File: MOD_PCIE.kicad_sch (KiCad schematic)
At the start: 1 part, among them J6 Bus_PCI_Express_Mini

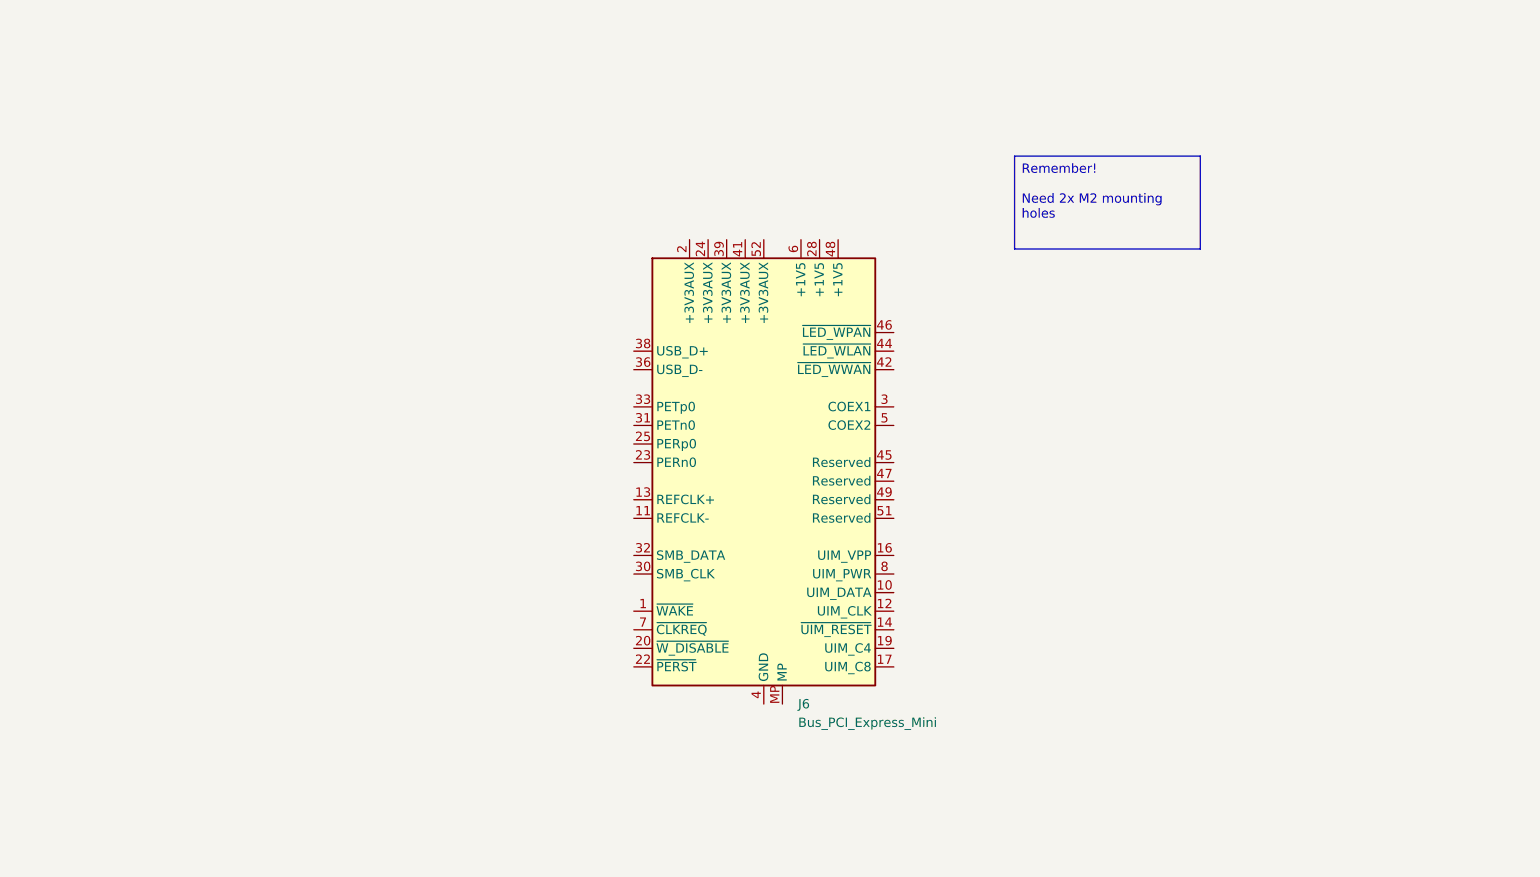
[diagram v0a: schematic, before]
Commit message: routed more sheets, improved analogs. next 5v /analog ground
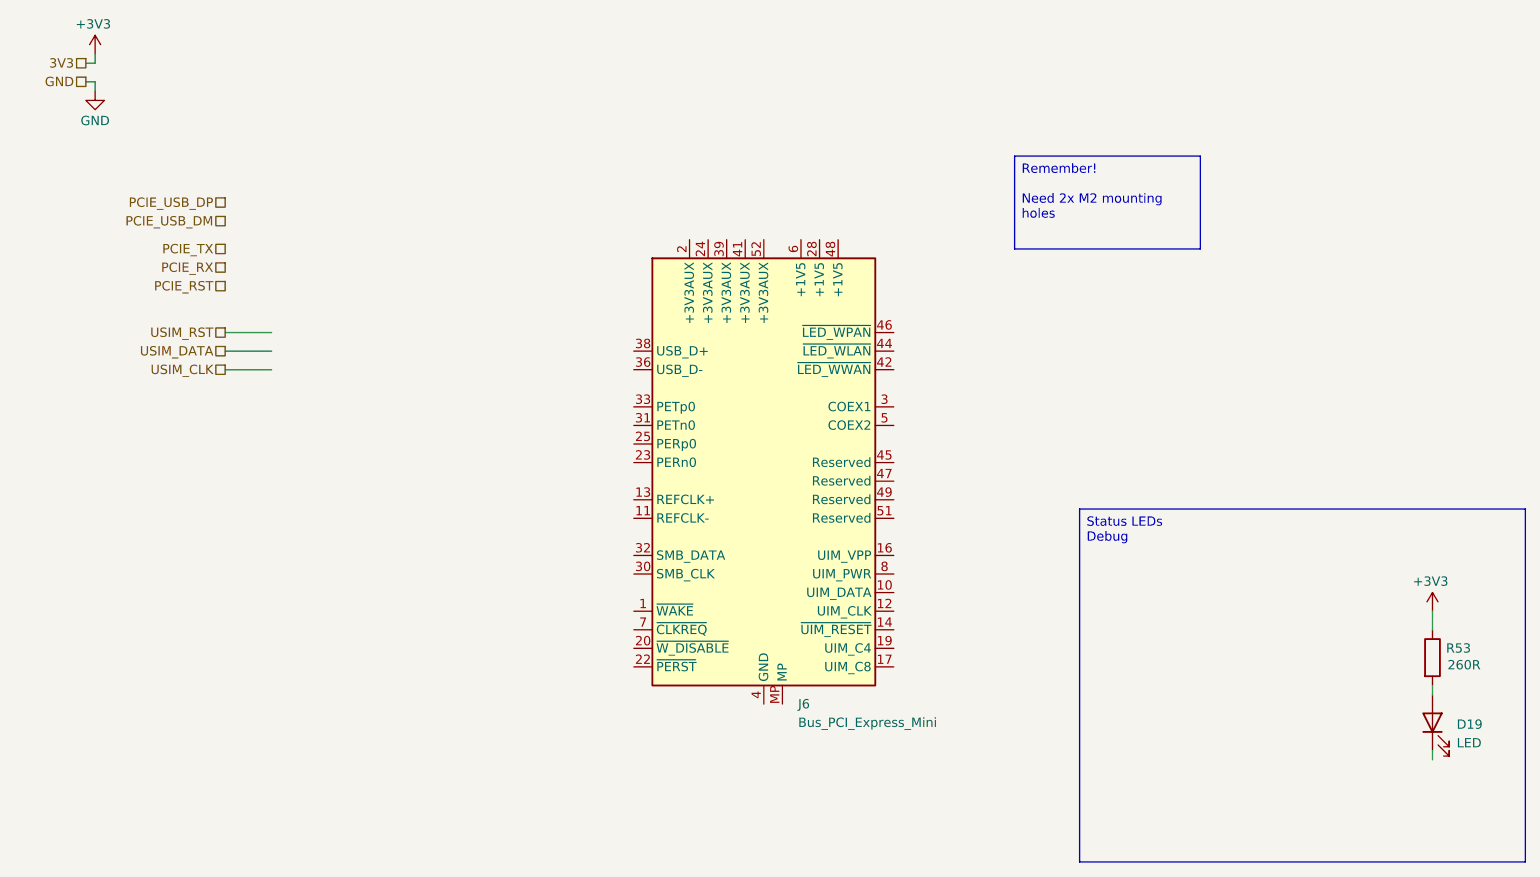
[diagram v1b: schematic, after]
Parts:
- added D19: LED, LED_SMD:LED_0603_1608Metric_Pad1.05x0.95mm_HandSolder, symbol Device:LED
- added R53: 260R, Resistor_SMD:R_0603_1608Metric_Pad0.98x0.95mm_HandSolder, symbol Device:R
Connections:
- new net: D19.2 (A), R53.2
- new net +3V3: R53.1

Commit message: added dip switches to wireless disables
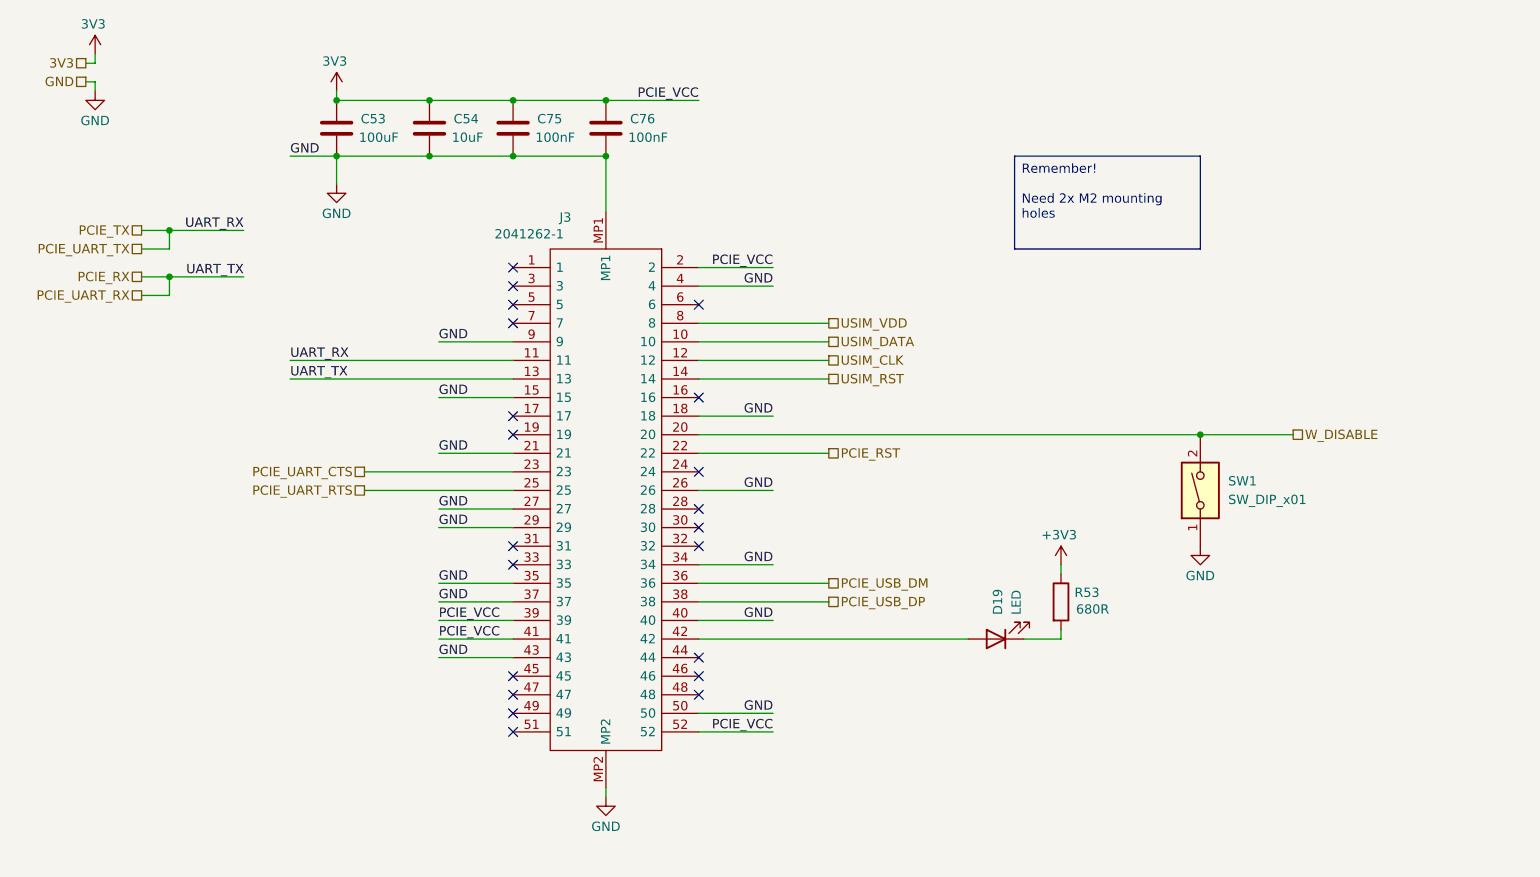
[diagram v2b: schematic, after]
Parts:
- removed J6: Bus_PCI_Express_Mini, Connector_PCBEdge:BUS_PCI_Express_Mini_Full, symbol Connector:Bus_PCI_Express_Mini
- added C53: 100uF, Capacitor_SMD:C_1210_3225Metric_Pad1.33x2.70mm_HandSolder, symbol Device:C
- added C54: 10uF, Capacitor_SMD:C_0603_1608Metric_Pad1.08x0.95mm_HandSolder, symbol Device:C
- added C75, C76: 100nF, Capacitor_SMD:C_0603_1608Metric_Pad1.08x0.95mm_HandSolder, symbol Device:C
- added J3: 2041262-1, 20412621, symbol 0_SamacSys_Parts:2041262-1
- added SW1: SW_DIP_x01, symbol Switch:SW_DIP_x01
- R53: value 260R -> 680R
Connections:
- net GND: now also C53.2, C54.2, C75.2, C76.2, J3.15, J3.18, J3.21, J3.26, J3.27, J3.29, J3.34, J3.35, J3.37, J3.4, J3.40, J3.43, J3.50, J3.9, J3.MP1, J3.MP2, SW1.1
- net PCIE_RST: now also J3.22
- net PCIE_RX: now also J3.13
- net PCIE_TX: now also J3.11
- net PCIE_USB_DM: now also J3.36
- net PCIE_USB_DP: now also J3.38
- net USIM_CLK: now also J3.12
- net USIM_DATA: now also J3.10
- net USIM_RST: now also J3.14
- net at D19.1 (K): now also R53.2
- net at D19.2 (A): now also J3.42; no longer R53.2
- new net 3V3: C53.1, C54.1, C75.1, C76.1, J3.2, J3.39, J3.41, J3.52
- new net PCIE_UART_CTS: J3.23
- new net PCIE_UART_RTS: J3.25
- new net USIM_VDD: J3.8
- new net W_DISABLE: J3.20, SW1.2
- no-connect marks 0 -> 21
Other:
- moved on the sheet: D19, R53

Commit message: redid annotations, added test point
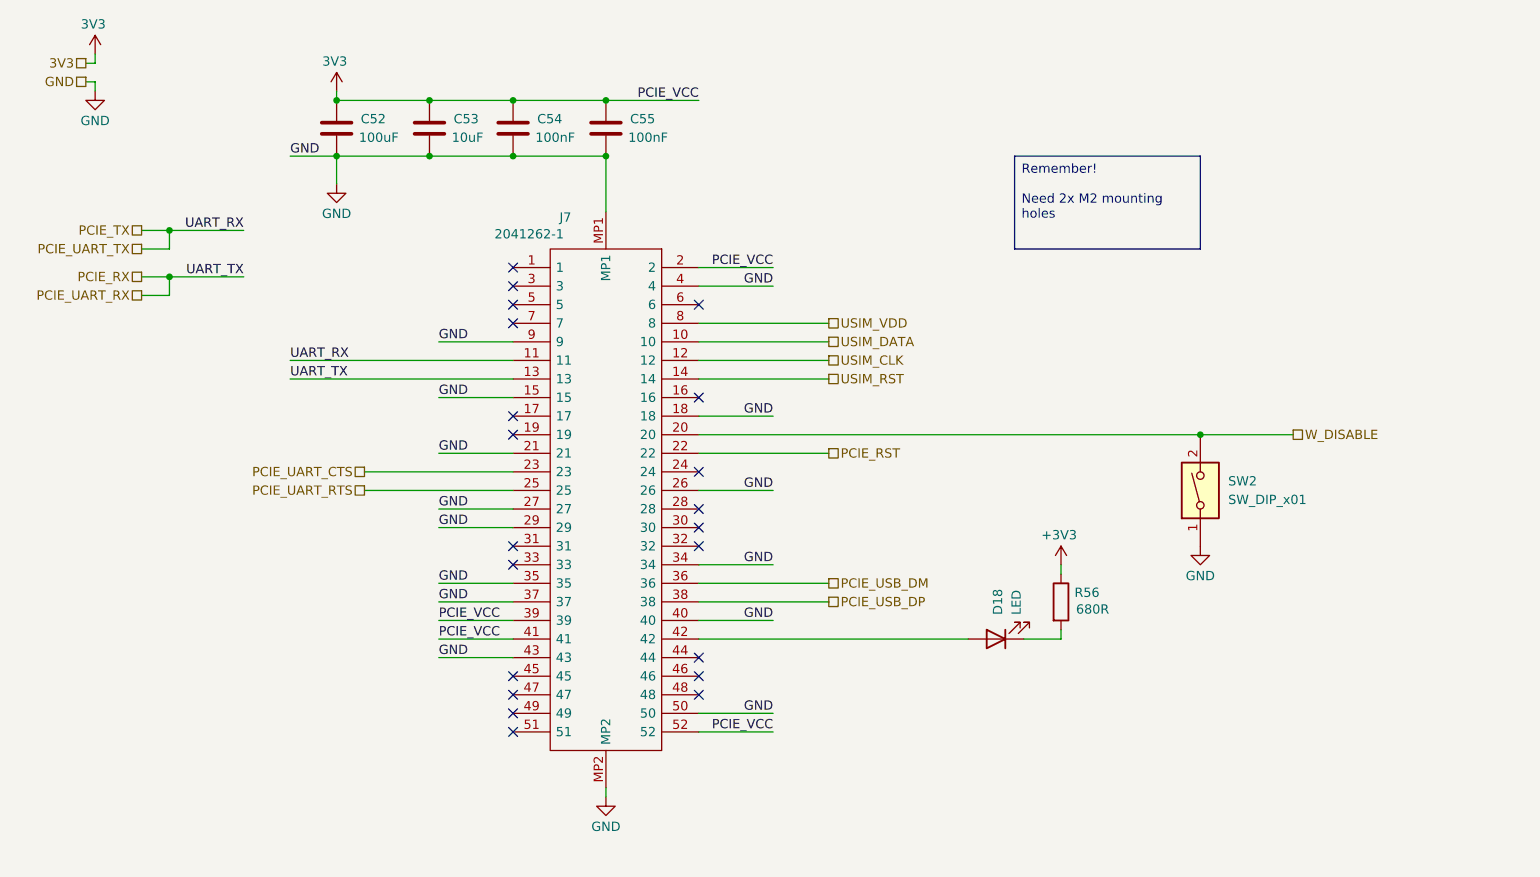
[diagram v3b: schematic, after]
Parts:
- SW2: renamed from SW1; footprint (none) -> SamacSys_Parts:DS01254L01BE
- renumbered C53 to C52, C54 to C53, C75 to C54, C76 to C55, D19 to D18, J3 to J7, R53 to R56
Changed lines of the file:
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@@
 		(on_board yes)
 		(dnp no)
-		(property "Reference" "J3"
+		(property "Reference" "J7"
 			(at 90.17 46.482 90)
 			(effects
@@
 			(project ""
 				(path "/3aee14c3-5480-4f7c-989e-3fef81779034/77f505d1-5a70-4b67-92f2-4570e0aae5e4"
-					(reference "J3")
+					(reference "J7")
 					(unit 1)
 				)
@@
 		(on_board yes)
 		(dnp no)
-		(property "Reference" "#PWR0135"
+		(property "Reference" "#PWR0223"
 			(at 26.67 35.56 0)
 			(effects
@@
 			(project "NCU"
 				(path "/3aee14c3-5480-4f7c-989e-3fef81779034/77f505d1-5a70-4b67-92f2-4570e0aae5e4"
-					(reference "#PWR0135")
+					(reference "#PWR0223")
 					(unit 1)
 				)
@@
 		(on_board yes)
 		(dnp no)
-		(property "Reference" "#PWR089"
+		(property "Reference" "#PWR0224"
 			(at 59.69 33.02 0)
 			(effects
@@
 			(project "NCU"
 				(path "/3aee14c3-5480-4f7c-989e-3fef81779034/77f505d1-5a70-4b67-92f2-4570e0aae5e4"
-					(reference "#PWR089")
+					(reference "#PWR0224")
 					(unit 1)
 				)
@@
 		(on_board yes)
 		(dnp no)
-		(property "Reference" "C53"
+		(property "Reference" "C52"
 			(at 62.992 33.02 0)
 			(effects
@@
 			(project "NCU"
 				(path "/3aee14c3-5480-4f7c-989e-3fef81779034/77f505d1-5a70-4b67-92f2-4570e0aae5e4"
-					(reference "C53")
+					(reference "C52")
 					(unit 1)
 				)
@@
 		(dnp no)
 		(fields_autoplaced yes)
-		(property "Reference" "SW1"
+		(property "Reference" "SW2"
 			(at 181.61 82.5499 90)
 			(effects
@@
 			)
 		)
-		(property "Footprint" ""
+		(property "Footprint" "SamacSys_Parts:DS01254L01BE"
 			(at 177.8 83.82 0)
 			(effects
@@
 			(project ""
 				(path "/3aee14c3-5480-4f7c-989e-3fef81779034/77f505d1-5a70-4b67-92f2-4570e0aae5e4"
-					(reference "SW1")
+					(reference "SW2")
 					(unit 1)
 				)
@@
 		(on_board yes)
 		(dnp no)
-		(property "Reference" "#PWR0307"
+		(property "Reference" "#PWR0227"
 			(at 96.52 132.08 0)
 			(effects
@@
 			(project "NCU"
 				(path "/3aee14c3-5480-4f7c-989e-3fef81779034/77f505d1-5a70-4b67-92f2-4570e0aae5e4"
-					(reference "#PWR0307")
+					(reference "#PWR0227")
 					(unit 1)
 				)
@@
 		(on_board yes)
 		(dnp no)
-		(property "Reference" "C54"
+		(property "Reference" "C53"
 			(at 75.692 33.02 0)
 			(effects
@@
 			(project "NCU"
 				(path "/3aee14c3-5480-4f7c-989e-3fef81779034/77f505d1-5a70-4b67-92f2-4570e0aae5e4"
-					(reference "C54")
+					(reference "C53")
 					(unit 1)
 				)
@@
 		(on_board yes)
 		(dnp no)
-		(property "Reference" "#PWR0311"
+		(property "Reference" "#PWR0230"
 			(at 177.8 97.79 0)
 			(effects
@@
 			(project "NCU"
 				(path "/3aee14c3-5480-4f7c-989e-3fef81779034/77f505d1-5a70-4b67-92f2-4570e0aae5e4"
-					(reference "#PWR0311")
+					(reference "#PWR0230")
 					(unit 1)
 				)
@@
 		(on_board yes)
 		(dnp no)
-		(property "Reference" "#PWR0308"
+		(property "Reference" "#PWR0225"
 			(at 59.69 48.26 0)
 			(effects
@@
 			(project "NCU"
 				(path "/3aee14c3-5480-4f7c-989e-3fef81779034/77f505d1-5a70-4b67-92f2-4570e0aae5e4"
-					(reference "#PWR0308")
+					(reference "#PWR0225")
 					(unit 1)
 				)
@@
 		(on_board yes)
 		(dnp no)
-		(property "Reference" "#PWR0134"
+		(property "Reference" "#PWR0221"
 			(at 26.67 27.94 0)
 			(effects
@@
 			(project "NCU"
 				(path "/3aee14c3-5480-4f7c-989e-3fef81779034/77f505d1-5a70-4b67-92f2-4570e0aae5e4"
-					(reference "#PWR0134")
+					(reference "#PWR0221")
 					(unit 1)
 				)
@@
 		(on_board yes)
 		(dnp no)
-		(property "Reference" "D19"
+		(property "Reference" "D18"
 			(at 150.114 100.838 90)
 			(effects
@@
 			(project "NCU"
 				(path "/3aee14c3-5480-4f7c-989e-3fef81779034/77f505d1-5a70-4b67-92f2-4570e0aae5e4"
-					(reference "D19")
+					(reference "D18")
 					(unit 1)
 				)
@@
 		(on_board yes)
 		(dnp no)
-		(property "Reference" "C75"
+		(property "Reference" "C54"
 			(at 87.122 33.02 0)
 			(effects
@@
 			(project "NCU"
 				(path "/3aee14c3-5480-4f7c-989e-3fef81779034/77f505d1-5a70-4b67-92f2-4570e0aae5e4"
-					(reference "C75")
+					(reference "C54")
 					(unit 1)
 				)
@@
 		(on_board yes)
 		(dnp no)
-		(property "Reference" "#PWR0146"
+		(property "Reference" "#PWR0229"
 			(at 158.75 97.79 0)
 			(effects
@@
 			(project "NCU"
 				(path "/3aee14c3-5480-4f7c-989e-3fef81779034/77f505d1-5a70-4b67-92f2-4570e0aae5e4"
-					(reference "#PWR0146")
+					(reference "#PWR0229")
 					(unit 1)
 				)
@@
 		(on_board yes)
 		(dnp no)
-		(property "Reference" "C76"
+		(property "Reference" "C55"
 			(at 99.822 33.02 0)
 			(effects
@@
 			(project "NCU"
 				(path "/3aee14c3-5480-4f7c-989e-3fef81779034/77f505d1-5a70-4b67-92f2-4570e0aae5e4"
-					(reference "C76")
+					(reference "C55")
 					(unit 1)
 				)
@@
 		(on_board yes)
 		(dnp no)
-		(property "Reference" "R53"
+		(property "Reference" "R56"
 			(at 162.306 97.79 0)
 			(effects
@@
 			(project "NCU"
 				(path "/3aee14c3-5480-4f7c-989e-3fef81779034/77f505d1-5a70-4b67-92f2-4570e0aae5e4"
-					(reference "R53")
-					(unit 1)
-				)
+					(reference "R56")
+					(unit 1)
+				)
